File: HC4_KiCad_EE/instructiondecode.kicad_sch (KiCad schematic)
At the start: 57 parts, among them IC10 74HC4002, IC18 74HC32, IC19 74HC74, IC20 74HC00, IC21 74HC4053, IC22 74HC04, IC23 74HC151

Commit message: 一部を整地
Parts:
- removed D10, D11, D12, D13, D14, D15, D16, D17, D18, D19, D2, D20, D21, D22, D23, D24, D25, D26, D27, D28, D29, D3, D30, D31, D32, D33, D34, D35, D36, D37, D38, D39, D4, D40, D41, D5, D6, D7, D8, D9: D, Library:DO-35_horizontal_anodeup_Smallhole, symbol Device:D
- removed IC10: 74HC4002, Package_DIP:DIP-14_W7.62mm_Socket, symbol 74xx_2:74HC4002
- removed IC18: 74HC32, Package_DIP:DIP-14_W7.62mm_Socket, symbol 74xx_2:74HC32
- removed unit 4 of IC20
- removed IC22: 74HC04, Package_DIP:DIP-14_W7.62mm_Socket, symbol 74xx_2:74HC04
- removed R5, R6: 10k, Resistor_THT:R_Axial_DIN0207_L6.3mm_D2.5mm_P7.62mm_Horizontal, symbol Device:R
- removed RN8: 10k, Resistor_THT:R_Array_SIP9, symbol Device:R_Network08_Split
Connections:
- net ~{ALU_OE} renamed Instruction_7
- no-connect marks 19 -> 5
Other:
- note removed: "I0a"
- note removed: "I1a"
- note removed: "I2a"
- note removed: "I3a"
- note removed: "MEMMode"
- note removed: "READ"
- note removed: "~{ALU_OE}"
- note removed: "~{Imm_OE}"
- note removed: "~{LevelC_OE}"
- note removed: "~{STACK_LE}"
- note removed: "~{is_JP_inst}"

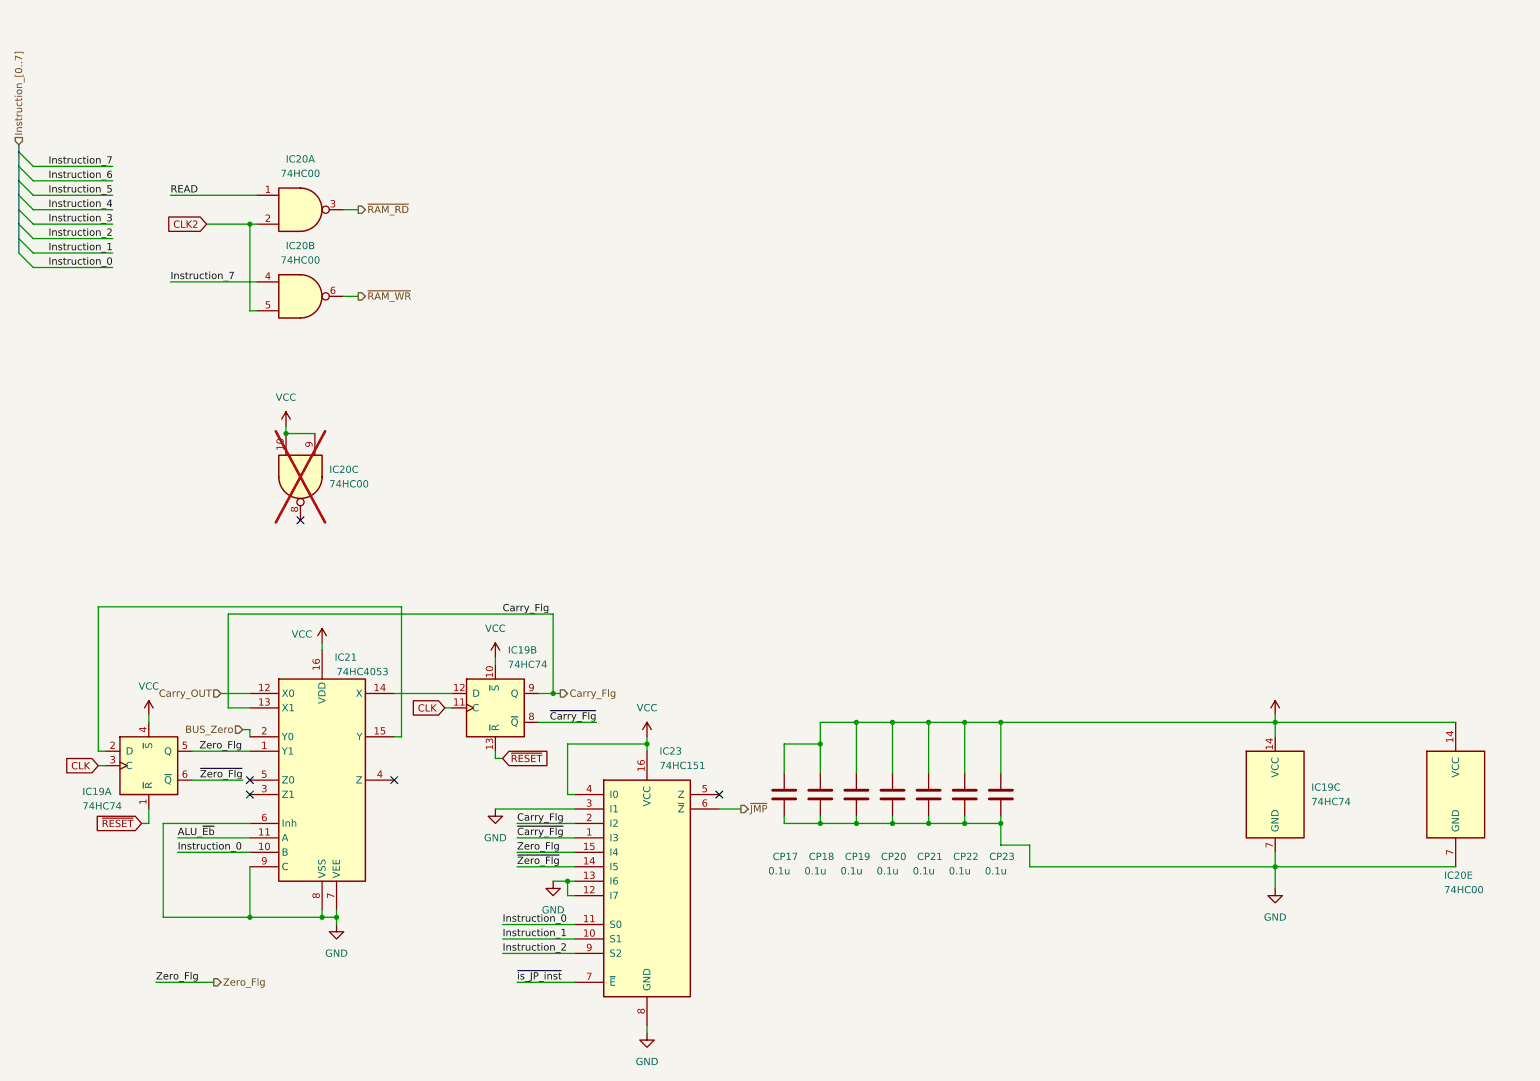
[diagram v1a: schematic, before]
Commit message: 4809を別シートに、ほか
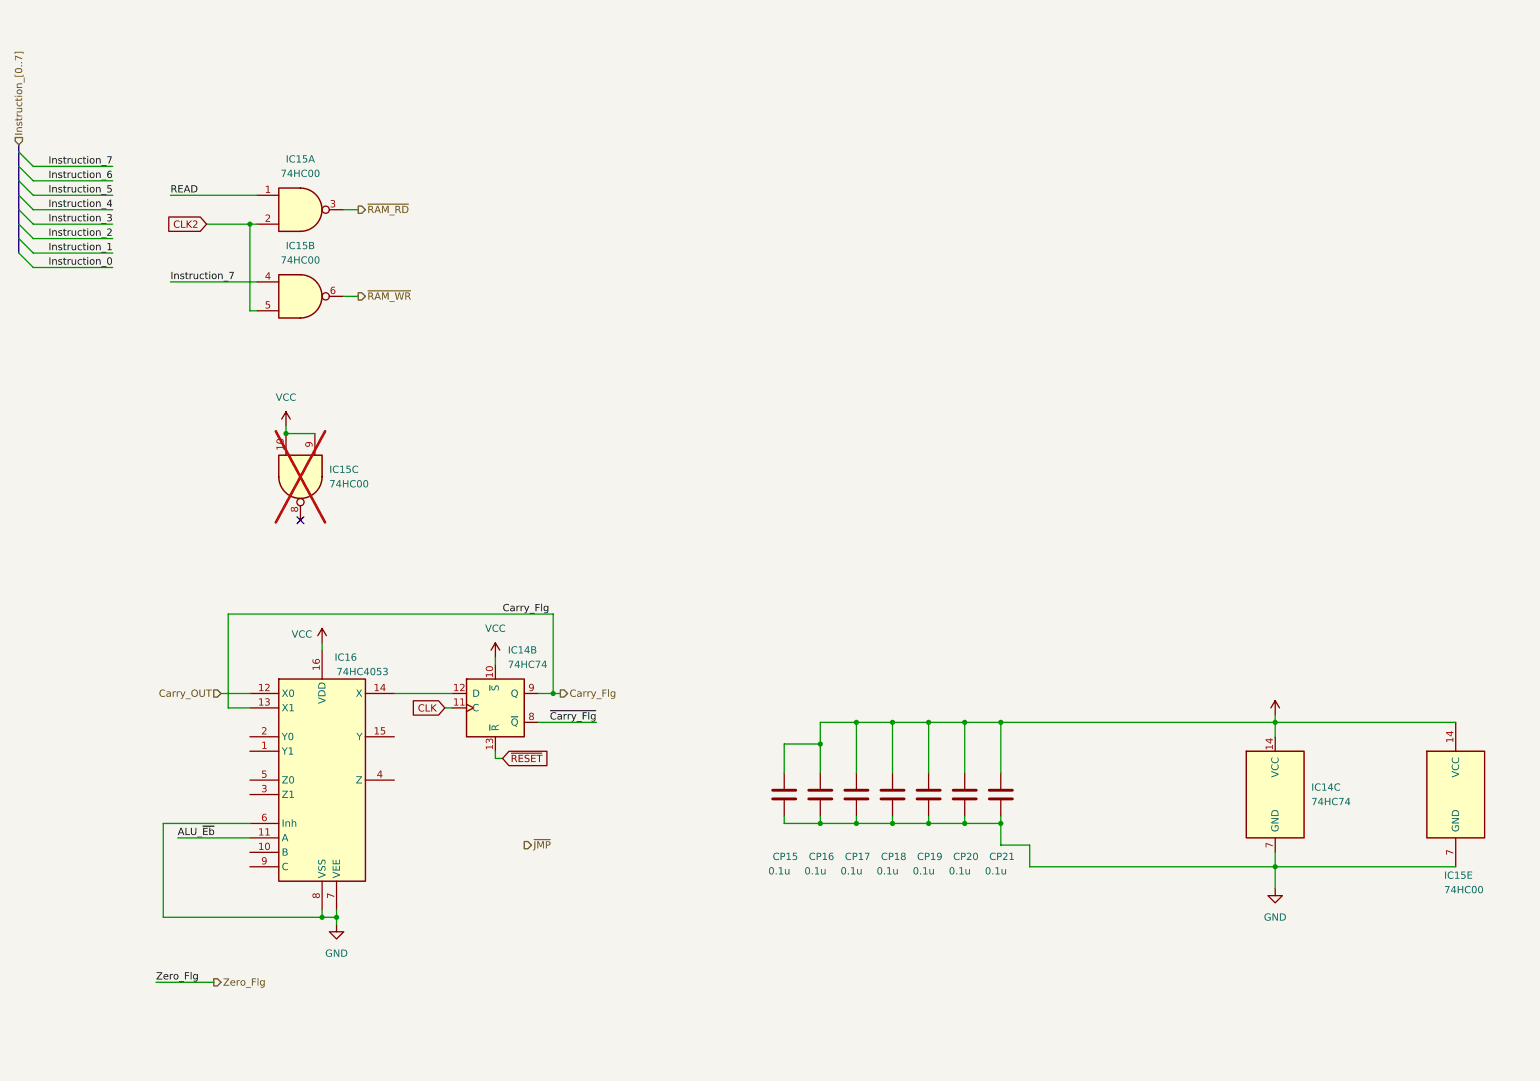
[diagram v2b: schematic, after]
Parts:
- removed unit 1 of IC19
- removed IC23: 74HC151, Package_DIP:DIP-16_W7.62mm_Socket, symbol 74xx_2:74HC151
- renumbered CP17 to CP15, CP18 to CP16, CP19 to CP17, CP20 to CP18, CP21 to CP19, CP22 to CP20, CP23 to CP21, IC19 to IC14, IC20 to IC15, IC21 to IC16
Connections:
- net GND: no longer IC16.9 (C)
- net Instruction_0: no longer IC16.10 (B)
- net Zero_Flg: no longer IC16.1 (Y1)
- net BUS_Zero: no longer names the net of IC16.2 (Y0)
- no-connect marks 5 -> 1

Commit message: 完成かも～
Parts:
- removed CP15, CP16, CP17: 0.1u, Capacitor_THT:C_Disc_D3.0mm_W1.6mm_P2.50mm, symbol Device2:C_Bypass
- added unit 4 of IC11
- added IC17: 74HC02, symbol 74xx_2:74HC02
- IC11: renamed from IC15; now fitted
- renumbered CP18 to CP17, CP19 to CP18, CP20 to CP19, CP21 to CP20, IC15 to IC11, IC16 to IC12, IC14 to IC13
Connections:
- net CLK: now also IC13.3 (C); no longer IC13.11 (C)
- net Carry_Flg: now also IC12.1 (Y1), IC13.5 (Q); no longer IC13.9 (Q)
- net GND: now also IC17.7 (GND)
- net Instruction_0: now also IC12.2 (Y0)
- net Instruction_1: now also IC12.10 (B)
- net Instruction_5: now also IC17.3
- net Instruction_6: now also IC11.10, IC17.2, IC17.9
- net Instruction_7: now also IC11.9, IC11.13, IC17.8
- net VCC: now also IC12.3 (Z1), IC13.4 (~{S}), IC17.14 (VCC); no longer IC11.10, IC11.9, IC13.10 (~{S})
- net ~{Carry_Flg}: now also IC13.6 (~{Q}); no longer IC13.8 (~{Q})
- net ~{JMP}: now also IC12.4 (Z)
- net ~{RESET}: now also IC13.1 (~{R}); no longer IC13.13 (~{R})
- net at IC13.12 (D): no longer IC12.14 (X)
- net at IC12.15 (Y): now also IC12.5 (Z0)
- net ~{Is_JP}: now reaches IC12.9 (C)
- net ~{Is_JP}: now also IC11.8, IC11.12
- net ALU_~{Eb} renamed ~{Carry_EN}
- net ~{Carry_EN}: now also IC17.13
- net READ renamed ~{ALU_OE}
- net ~{ALU_OE}: now also IC17.1
- new net: IC17.10, IC17.11, IC17.12
- new net: IC12.14 (X), IC13.2 (D)
- new net ~{STACK_LE}: IC11.11
- no-connect marks 1 -> 0
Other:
- moved on the sheet: IC11E

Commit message: Carry_ENを論理反転、回路図の修正
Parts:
- removed unit 4 of IC17
- added unit 4 of IC11
- added unit 2 of IC11
- added unit 2 of IC14
- added LD32, LD33, LD34, LD35, LD36, LD37, LD38: Chip, symbol Device2:LED_
- added R10, R4, R5, R6, R7, R8, R9: 1k, symbol Device:R
- renumbered CP17 to CP14, CP18 to CP15, CP19 to CP16, CP20 to CP17, IC17 to IC11, IC11 to IC12, IC12 to IC13, IC13 to IC14
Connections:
- net ~{Carry_EN} is gone; now on net Carry_EN: IC13.11 (A)
- net Carry_Flg: now also IC13.12 (X0); no longer IC13.13 (X1)
- net Carry_OUT: now also IC13.13 (X1); no longer IC13.12 (X0)
- net GND: now also R10.2, R4.2, R5.2, R6.2, R7.2, R8.2, R9.2
- net VCC: now also IC11.11, IC11.12, IC11.5, IC11.6, IC14.10 (~{S}), IC14.11 (C), IC14.12 (D), IC14.13 (~{R})
- net ~{ALU_OE}: now also LD34.2
- net ~{Is_JP}: now also LD32.2
- net ~{JMP}: now also LD35.2
- net ~{RAM_RD}: now also LD37.2
- net ~{RAM_WR}: now also LD36.2
- net ~{STACK_LE}: now also LD38.2
- net Carry_EN: now reaches IC11.10
- net Carry_EN: now also LD33.2
- new net: LD32.1 (K), R4.1
- new net: LD33.1 (K), R5.1
- new net: LD36.1 (K), R8.1
- new net: LD35.1 (K), R7.1
- new net: LD37.1 (K), R9.1
- new net: LD38.1 (K), R10.1
- new net: LD34.1 (K), R6.1
- no-connect marks 0 -> 4

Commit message: PortBを4511に、フットプリントの割り付け開始
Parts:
- CP14, CP15, CP16, CP17: footprint Capacitor_THT:C_Disc_D3.0mm_W1.6mm_P2.50mm -> Capacitor_SMD:C_0603_1608Metric
- IC11: footprint (none) -> Package_SO:SO-14_5.3x10.2mm_P1.27mm
- IC12, IC14: footprint Package_DIP:DIP-14_W7.62mm_Socket -> Package_SO:SO-14_5.3x10.2mm_P1.27mm
- IC13: footprint Package_DIP:DIP-16_W7.62mm_Socket -> Package_SO:SO-16_5.3x10.2mm_P1.27mm
- renumbered R4 to R11, R5 to R12, R6 to R13, R7 to R14, R8 to R15, R9 to R16, R10 to R17
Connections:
- net Instruction_0 renamed Data_A0
- net Instruction_1 renamed Data_A1
- net ~{Carry_Flg}: no longer names the net of IC14.6 (~{Q})
- no-connect marks 4 -> 5
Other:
- note added: "~{Carry_Flg}"

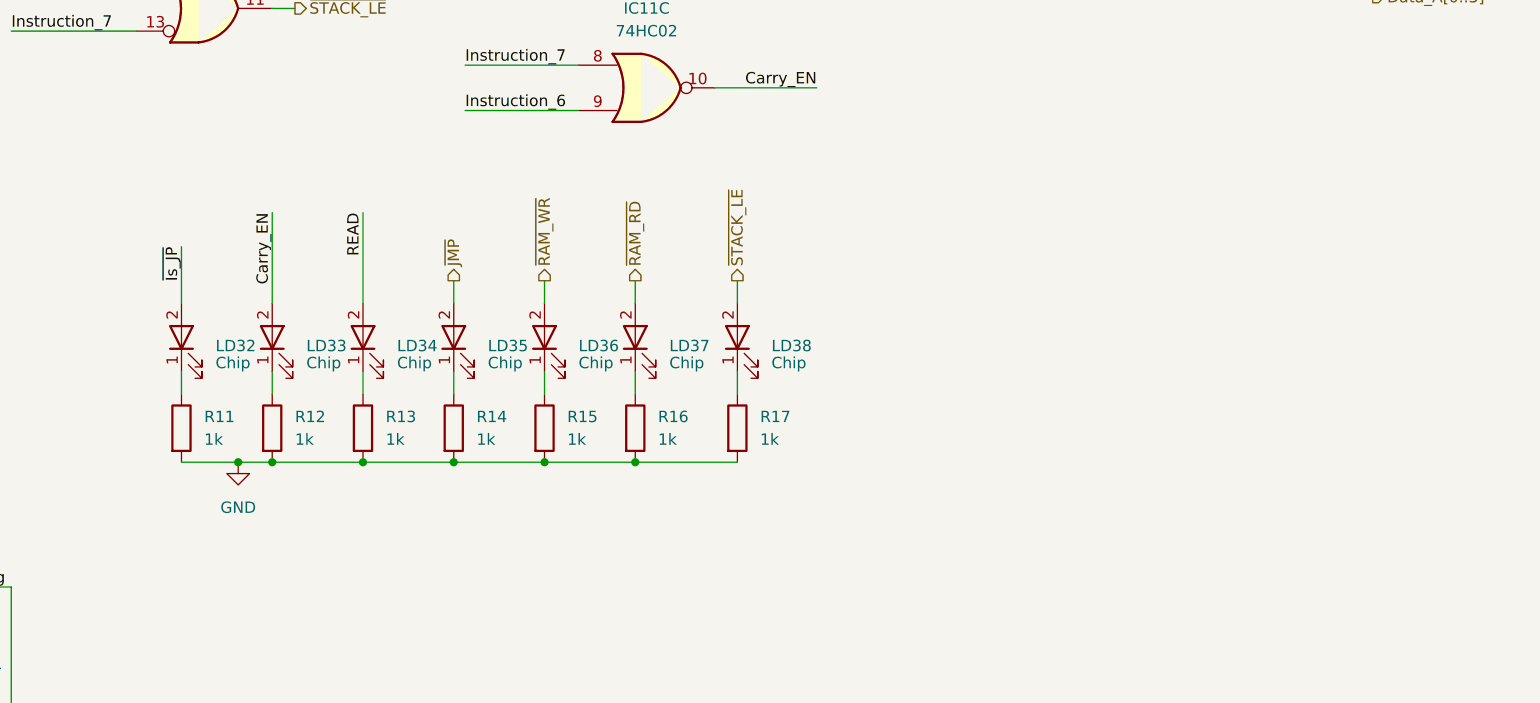
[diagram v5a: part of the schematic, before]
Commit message: チップ集合抵抗に変更、基板作成開始
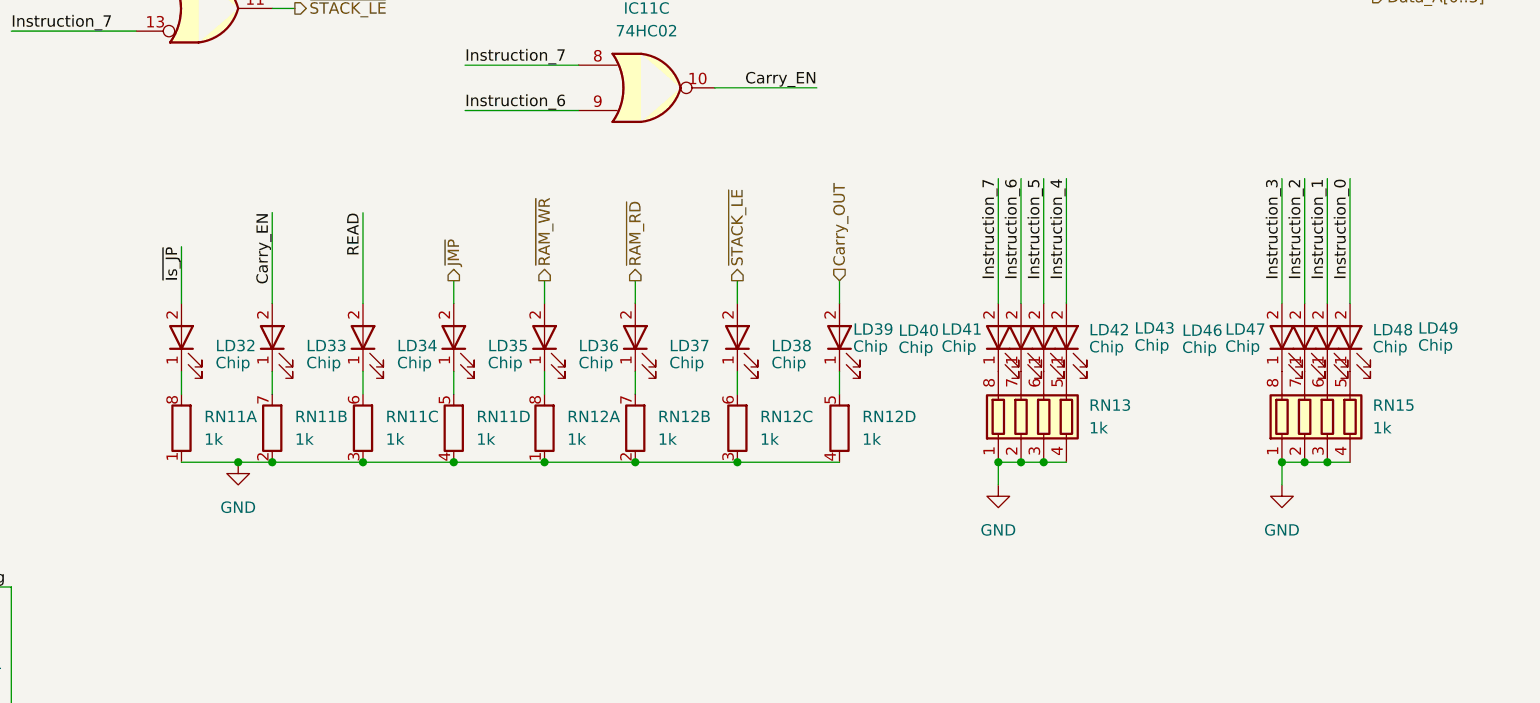
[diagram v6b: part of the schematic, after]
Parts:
- removed R11, R12, R13, R14, R15, R16, R17: 1k, symbol Device:R
- added LD39, LD40, LD41, LD42, LD43, LD46, LD47, LD48, LD49: Chip, LED_SMD:LED_0603_1608Metric, symbol Device2:LED_
- added RN11, RN12: 1k, Resistor_SMD:R_Array_Convex_4x0603, symbol Device:R_Pack04_Split
- added RN13, RN15: 1k, Resistor_SMD:R_Array_Convex_4x0603, symbol Device:R_Pack04
- LD32, LD33, LD34, LD35, LD36, LD37, LD38: footprint (none) -> LED_SMD:LED_0603_1608Metric
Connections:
- net Carry_OUT: now also LD39.2
- net Data_A0: now also LD49.2
- net Data_A1: now also LD48.2
- net Data_A2: now also LD47.2
- net Data_A3: now also LD46.2
- net GND: now also RN11.1 (R1.1), RN11.2 (R2.1), RN11.3 (R3.1), RN11.4 (R4.1), RN12.1 (R1.1), RN12.2 (R2.1), RN12.3 (R3.1), RN12.4 (R4.1), RN13.1 (R1.1), RN13.2 (R2.1), RN13.3 (R3.1), RN13.4 (R4.1), RN15.1 (R1.1), RN15.2 (R2.1), RN15.3 (R3.1), RN15.4 (R4.1)
- net Instruction_4: now also LD43.2
- net Instruction_5: now also LD42.2
- net Instruction_6: now also LD41.2
- net Instruction_7: now also LD40.2
- net at LD32.1 (K): now also RN11.8 (R1.2)
- net at LD33.1 (K): now also RN11.7 (R2.2)
- net at LD36.1 (K): now also RN12.8 (R1.2)
- net at LD35.1 (K): now also RN11.5 (R4.2)
- net at LD37.1 (K): now also RN12.7 (R2.2)
- net at LD38.1 (K): now also RN12.6 (R3.2)
- net at LD34.1 (K): now also RN11.6 (R3.2)
- new net: LD49.1 (K), RN15.5 (R4.2)
- new net: LD48.1 (K), RN15.6 (R3.2)
- new net: LD43.1 (K), RN13.5 (R4.2)
- new net: LD40.1 (K), RN13.8 (R1.2)
- new net: LD42.1 (K), RN13.6 (R3.2)
- new net: LD41.1 (K), RN13.7 (R2.2)
- new net: LD39.1 (K), RN12.5 (R4.2)
- new net: LD47.1 (K), RN15.7 (R2.2)
- new net: LD46.1 (K), RN15.8 (R1.2)
